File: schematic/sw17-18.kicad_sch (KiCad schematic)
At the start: 2 parts, among them SW17 SW_Push, SW18 SW_Push

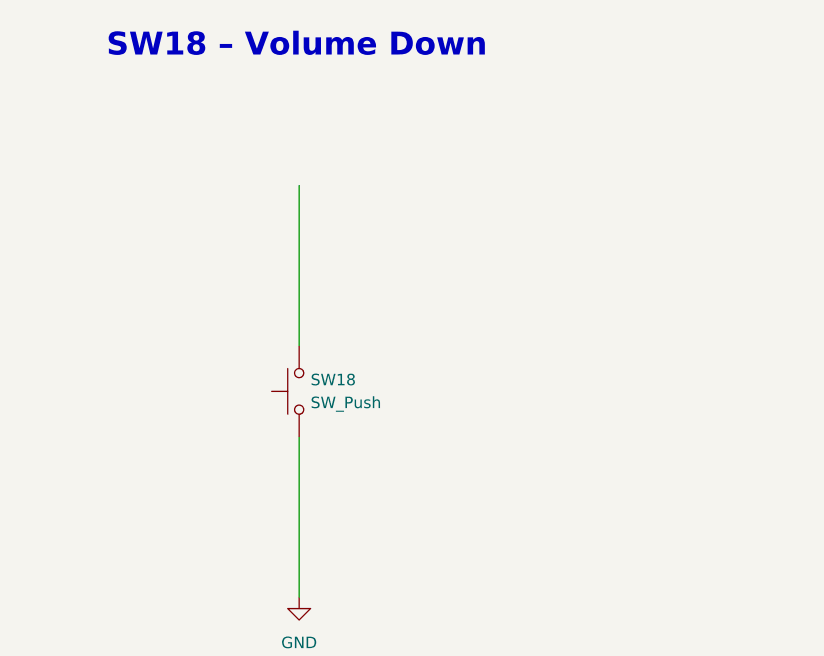
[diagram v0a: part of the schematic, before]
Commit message: Added J5 and assoc. resistor network. Added traceable signals for MYSTERY_SIG
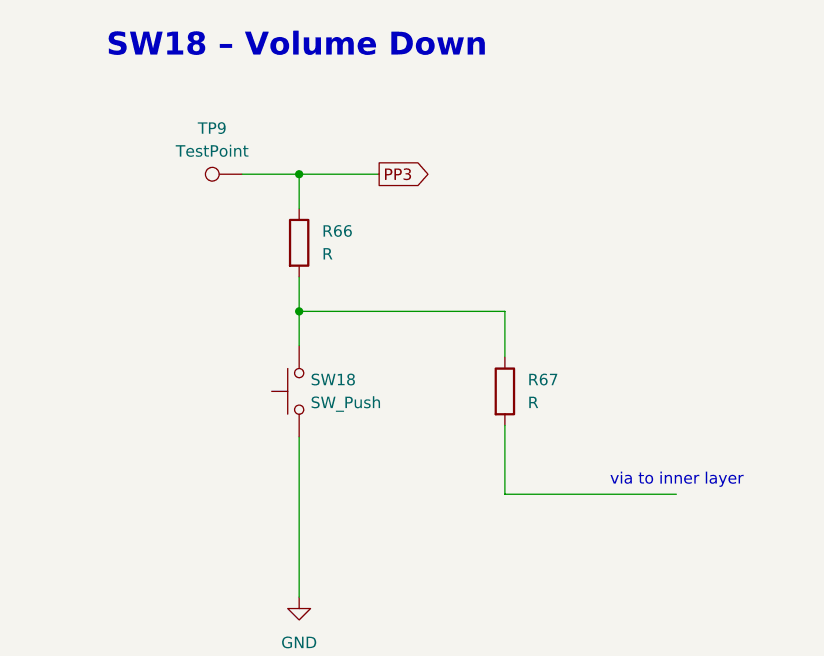
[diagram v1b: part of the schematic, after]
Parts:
- added R66, R67: R, symbol Device:R
- added TP9: TestPoint, symbol Connector:TestPoint
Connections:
- net at SW18.2: now also R66.2, R67.1
- new net PP3: R66.1, TP9.1
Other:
- note added: "via to inner layer"
